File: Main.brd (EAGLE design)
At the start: 92.2 x 102.4 mm, 41 parts, among them IC1 7805T, IC2 LD117AV33, IC3 LM35CZ, Q1 IRLZ44N, T1 2N3904, U1 PIC18F45K22-I/P

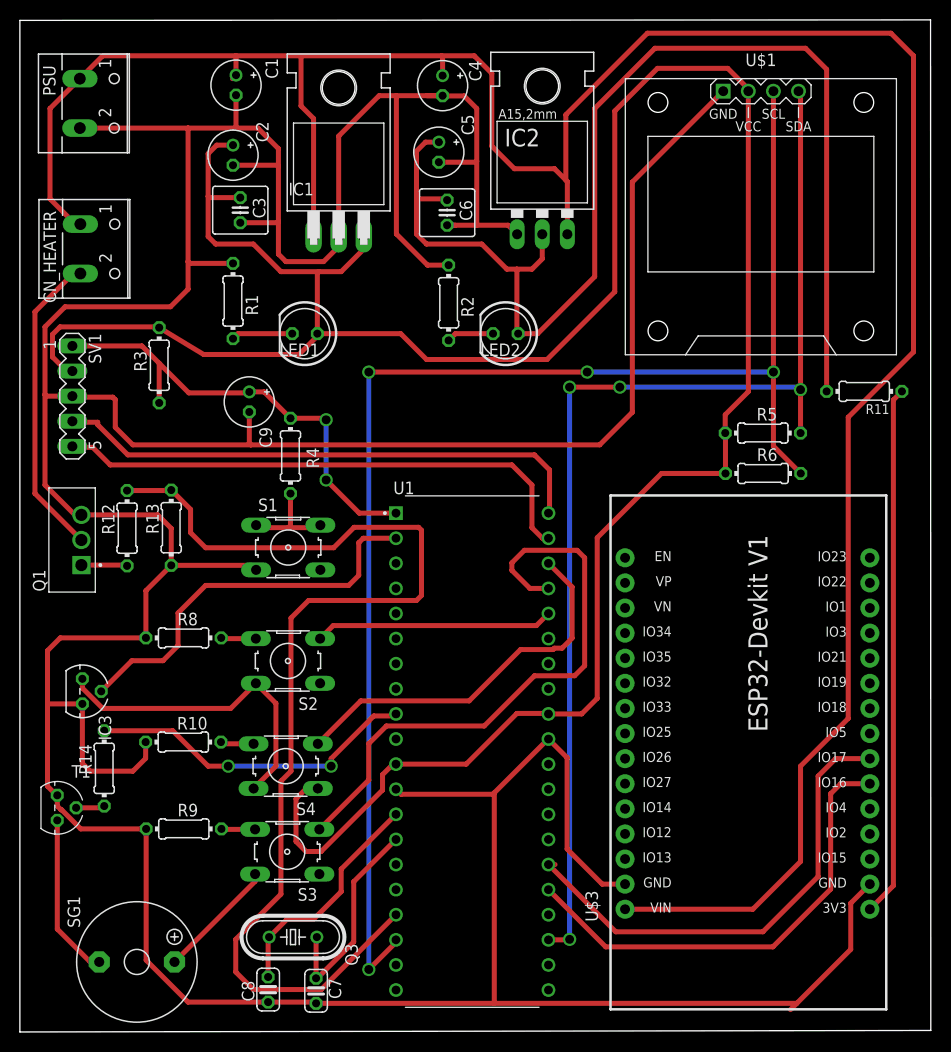
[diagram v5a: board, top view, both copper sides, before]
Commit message: Routing complete, Checking routes and design
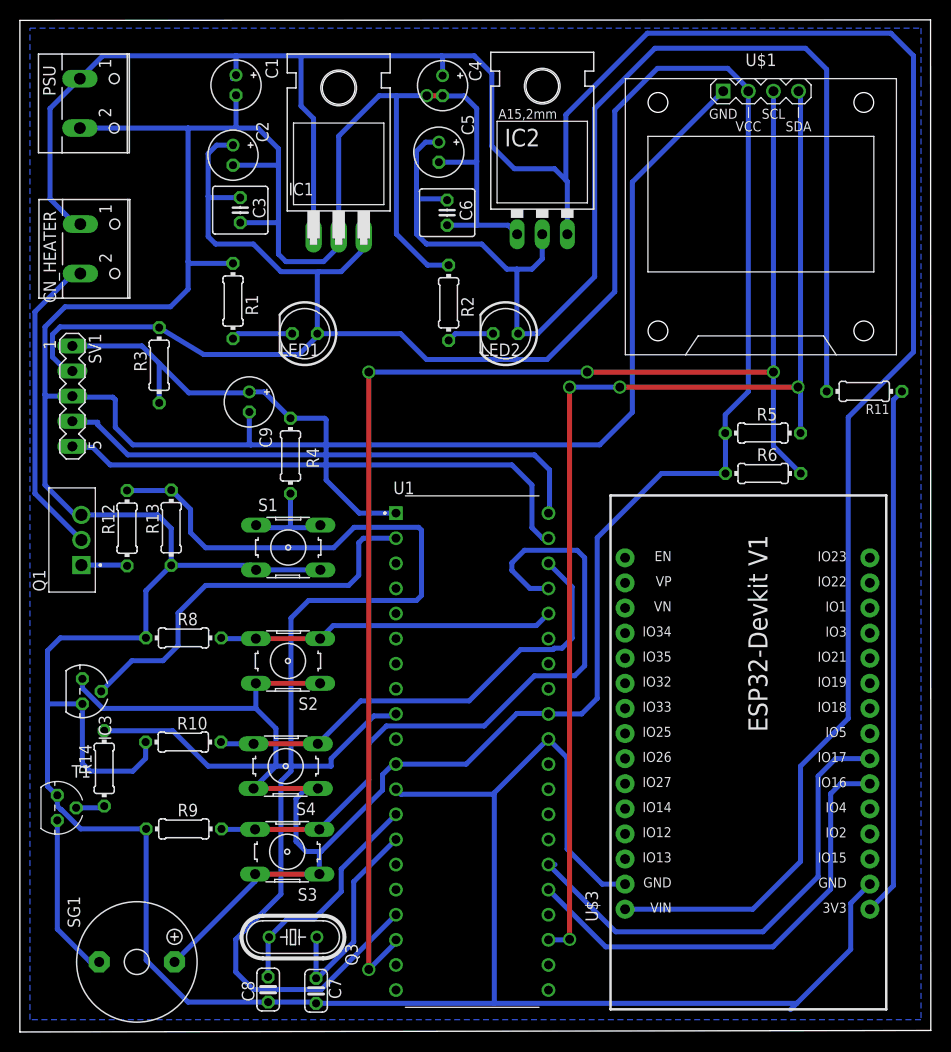
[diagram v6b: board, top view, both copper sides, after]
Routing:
- net VCC: track 305.4 -> 326.2 mm
- net DIN_LOCAL_REMOTE: track 27.7 -> 34.2 mm
- net DIN_BUTTON_UP: track 63.6 -> 70.1 mm
- net DIN_BUTTON_DOWN: track 42.1 -> 48.6 mm
- net GND: track 527.8 -> 533.1 mm, vias 0 -> 1
- net +12V: vias 0 -> 1
- net DOUT_BUZZER: vias 2 -> 0
- net MCLR: vias 2 -> 0
- added copper zone on layer 16, net GND

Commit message: Ready to deliver
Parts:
- CN_HEATER: value PSU -> HEATER
- Q3: value (none) -> 20MHz
- S2: value (none) -> LOCAL/REMOTE
- S3: value (none) -> UP
- S4: value (none) -> DOWN
- renumbered SG1 to BUZZER
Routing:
- net GND: track 533.1 -> 534.0 mm

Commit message: Ready to deliver
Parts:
- S1: value (none) -> RESET
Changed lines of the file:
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@@
 <layer number="40" name="bKeepout" color="1" fill="11" visible="no" active="yes"/>
 <layer number="41" name="tRestrict" color="4" fill="10" visible="no" active="yes"/>
-<layer number="42" name="bRestrict" color="1" fill="10" visible="yes" active="yes"/>
+<layer number="42" name="bRestrict" color="1" fill="10" visible="no" active="yes"/>
 <layer number="43" name="vRestrict" color="2" fill="10" visible="no" active="yes"/>
-<layer number="44" name="Drills" color="7" fill="1" visible="no" active="yes"/>
+<layer number="44" name="Drills" color="7" fill="1" visible="yes" active="yes"/>
 <layer number="45" name="Holes" color="7" fill="1" visible="yes" active="yes"/>
 <layer number="46" name="Milling" color="3" fill="1" visible="no" active="yes"/>
@@
 <attribute name="VALUE" x="18.3388" y="6.2484" size="1.27" layer="27" ratio="10"/>
 </element>
-<element name="S1" library="switch-omron" library_urn="urn:adsk.eagle:library:377" package="B3F-10XX" package3d_urn="urn:adsk.eagle:package:27496/1" value="" x="27.1526" y="48.7934" smashed="yes">
+<element name="S1" library="switch-omron" library_urn="urn:adsk.eagle:library:377" package="B3F-10XX" package3d_urn="urn:adsk.eagle:package:27496/1" value="RESET" x="27.1526" y="48.7934" smashed="yes">
 <attribute name="MF" value="" x="27.1526" y="48.7934" size="1.778" layer="27" display="off"/>
 <attribute name="MPN" value="B3F-1000" x="27.1526" y="48.7934" size="1.778" layer="27" display="off"/>
-<attribute name="NAME" x="24.1046" y="52.4764" size="1.27" layer="25" ratio="10"/>
+<attribute name="NAME" x="31.9786" y="48.1584" size="1.27" layer="25" ratio="10"/>
 <attribute name="OC_FARNELL" value="176432" x="27.1526" y="48.7934" size="1.778" layer="27" display="off"/>
 <attribute name="OC_NEWARK" value="36M3542" x="27.1526" y="48.7934" size="1.778" layer="27" display="off"/>
 <attribute name="POPULARITY" value="72" x="27.1526" y="48.7934" size="1.778" layer="27" display="off"/>
-<attribute name="VALUE" x="24.1046" y="43.7134" size="1.27" layer="27" ratio="10"/>
+<attribute name="VALUE" x="24.3586" y="52.0954" size="1.27" layer="27" ratio="10"/>
 </element>
 <element name="S2" library="switch-omron" library_urn="urn:adsk.eagle:library:377" package="B3F-10XX" package3d_urn="urn:adsk.eagle:package:27496/1" value="LOCAL/REMOTE" x="27.1272" y="37.3126" smashed="yes" rot="R180">
@@
 <attribute name="OC_NEWARK" value="36M3542" x="27.1272" y="37.3126" size="1.778" layer="27" rot="R180" display="off"/>
 <attribute name="POPULARITY" value="72" x="27.1272" y="37.3126" size="1.778" layer="27" rot="R180" display="off"/>
-<attribute name="VALUE" x="34.2392" y="42.1386" size="1.27" layer="27" ratio="10" rot="R180"/>
+<attribute name="VALUE" x="20.3708" y="40.6654" size="1.27" layer="27" ratio="10"/>
 </element>
 <element name="S3" library="switch-omron" library_urn="urn:adsk.eagle:library:377" package="B3F-10XX" package3d_urn="urn:adsk.eagle:package:27496/1" value="UP" x="27.051" y="18.0086" smashed="yes" rot="R180">
